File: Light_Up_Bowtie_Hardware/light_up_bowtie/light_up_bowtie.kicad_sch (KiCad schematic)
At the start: 17 parts, among them SW1 SW_SPDT, U1 ATtiny85-20S

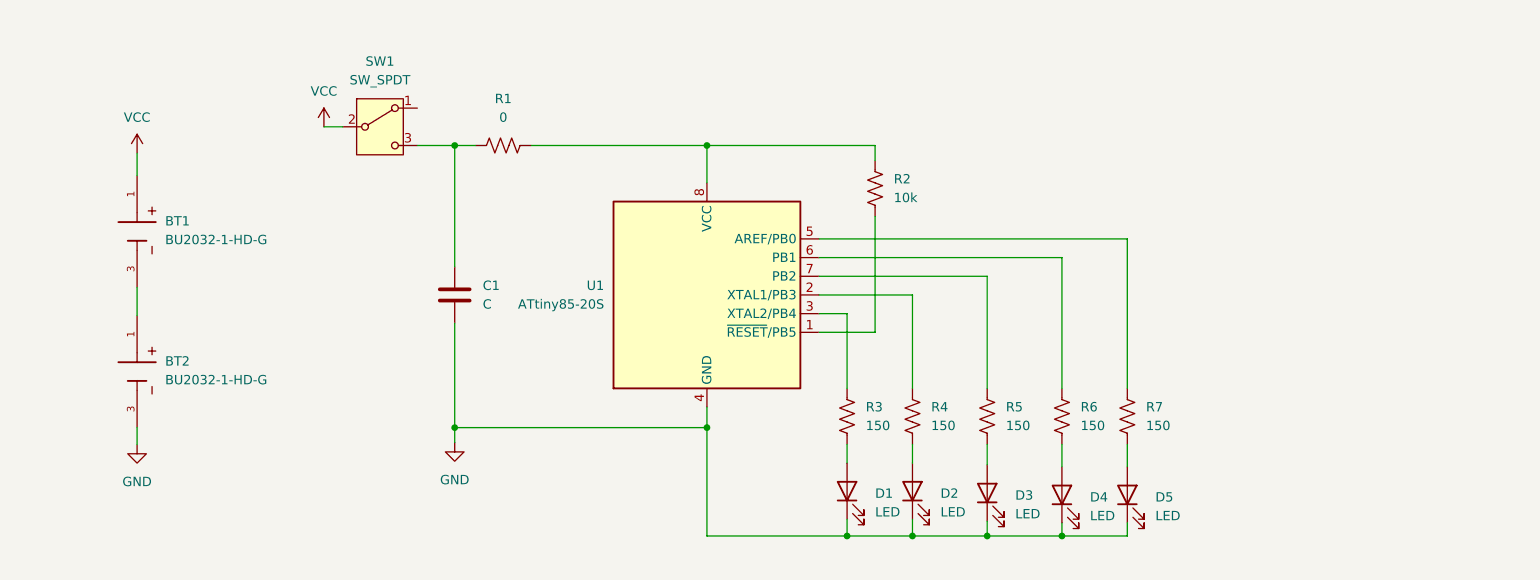
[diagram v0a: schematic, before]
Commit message: Added DNI lipo circuitry and programming header
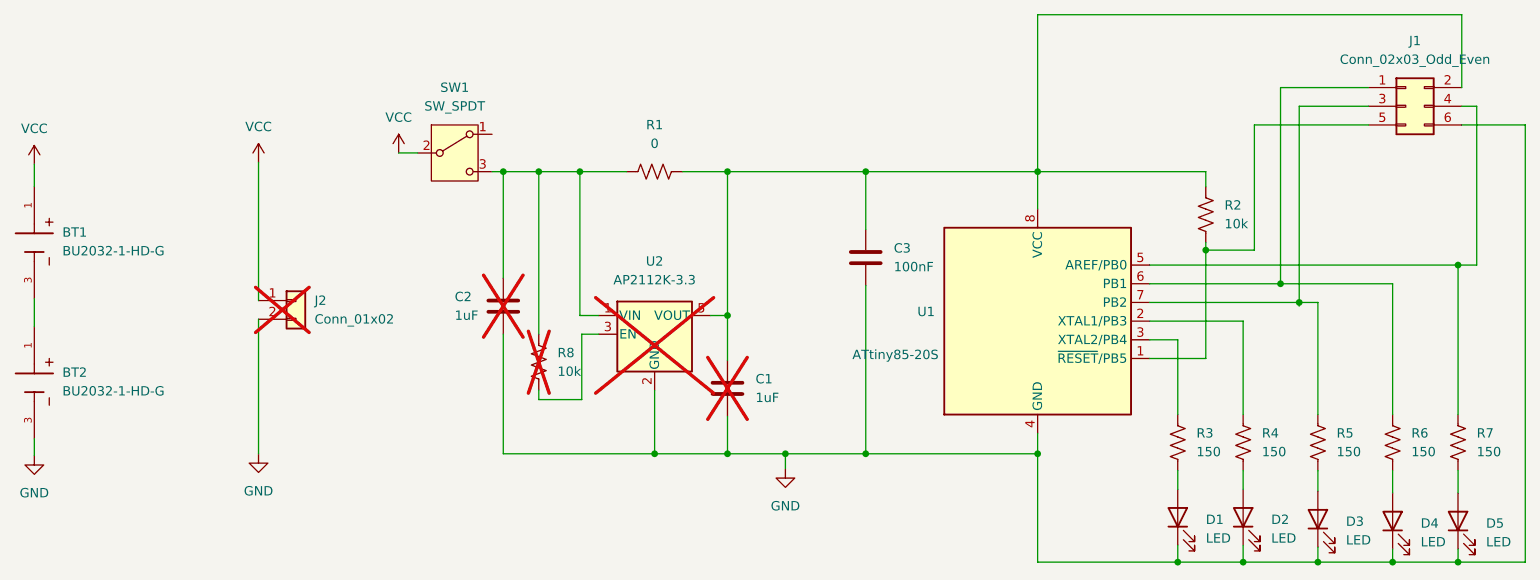
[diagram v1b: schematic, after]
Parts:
- added C2: 1uF, Capacitor_SMD:C_0402_1005Metric_Pad0.74x0.62mm_HandSolder, symbol Device:C
- added C3: 100nF, Capacitor_SMD:C_0402_1005Metric_Pad0.74x0.62mm_HandSolder, symbol Device:C
- added J1: Conn_02x03_Odd_Even, symbol Connector_Generic:Conn_02x03_Odd_Even
- added J2: Conn_01x02, symbol Connector_Generic:Conn_01x02
- added R8: 10k, symbol Device:R_US
- added U2: AP2112K-3.3, Package_TO_SOT_SMD:SOT-23-5, symbol Regulator_Linear:AP2112K-3.3
- C1: value C -> 1uF; now not fitted
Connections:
- net GND: now also C2.2, C3.2, J1.6 (Pin_6), J2.2 (Pin_2), U2.2 (GND)
- net VCC: now also J2.1 (Pin_1)
- net at R2.2, U1.1 (~{RESET}/PB5): now also J1.5 (Pin_5)
- net at R7.1, U1.5 (AREF/PB0): now also J1.4 (Pin_4)
- net at R6.1, U1.6 (PB1): now also J1.1 (Pin_1)
- net at R5.1, U1.7 (PB2): now also J1.3 (Pin_3)
- net at R1.2, R2.1, U1.8 (VCC): now also C1.1, C3.1, J1.2 (Pin_2), U2.5 (VOUT)
- net at R1.1, SW1.3 (C): now also C2.1, R8.1, U2.1 (VIN); no longer C1.1
- new net: R8.2, U2.3 (EN)
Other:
- moved on the sheet: BT1, BT2, D1, D2, D3, D4, D5, R1, R2, R3, R4, R5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

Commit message: Assigned footprints, added board shape, initial placement
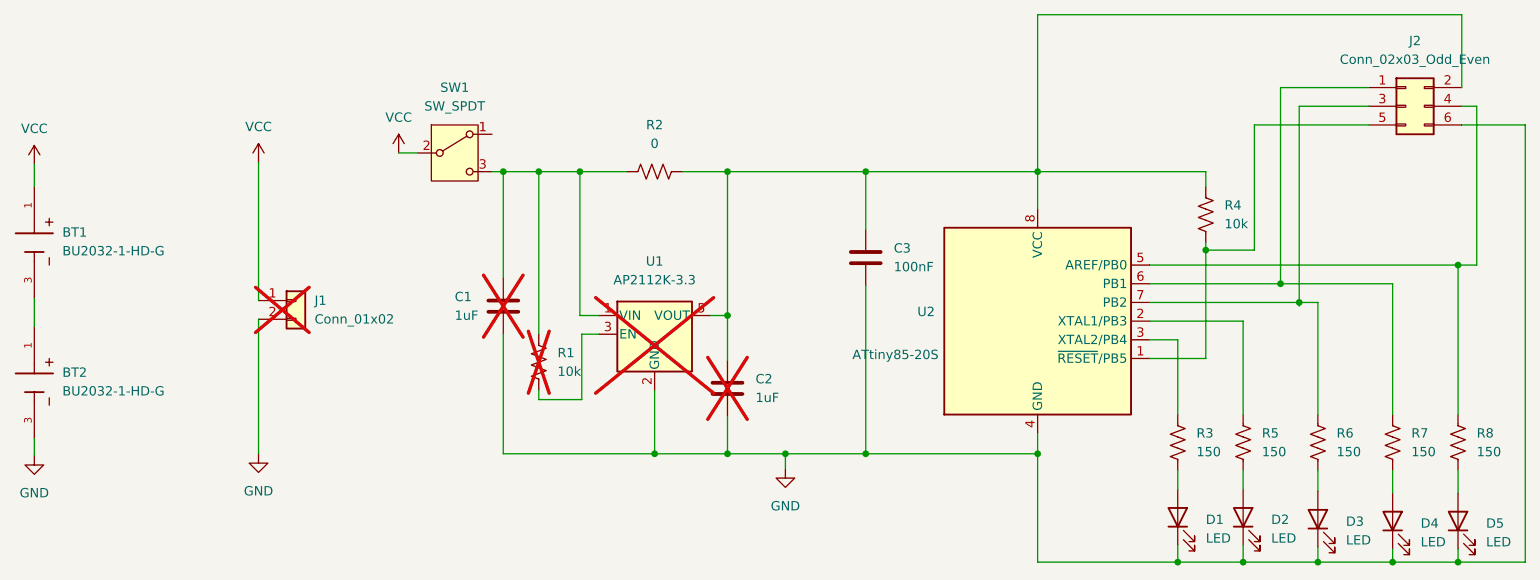
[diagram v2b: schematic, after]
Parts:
- J1: renamed from J2; footprint (none) -> Connector_JST:JST_PH_S2B-PH-K_1x02_P2.00mm_Horizontal
- J2: renamed from J1; footprint (none) -> Connector_PinHeader_2.54mm:PinHeader_2x03_P2.54mm_Vertical
- R1: renamed from R8; footprint (none) -> Resistor_SMD:R_0603_1608Metric_Pad0.98x0.95mm_HandSolder
- renumbered C2 to C1, C1 to C2, R1 to R2, R2 to R4, R4 to R5, R5 to R6, R6 to R7, R7 to R8, U2 to U1, U1 to U2
